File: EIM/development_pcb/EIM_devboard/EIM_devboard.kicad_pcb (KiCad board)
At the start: 2 copper layers, 100 x 100 mm, 114 parts, among them IC1 TPL7407LADR, IC2 MC33660BEFR2, J1 MX34028NF2, J2 Relays, J3 FTDI, J4 DB9_Male, J5 CAN, Q1 2N7000, Q10 2N7000, Q2 2N7000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

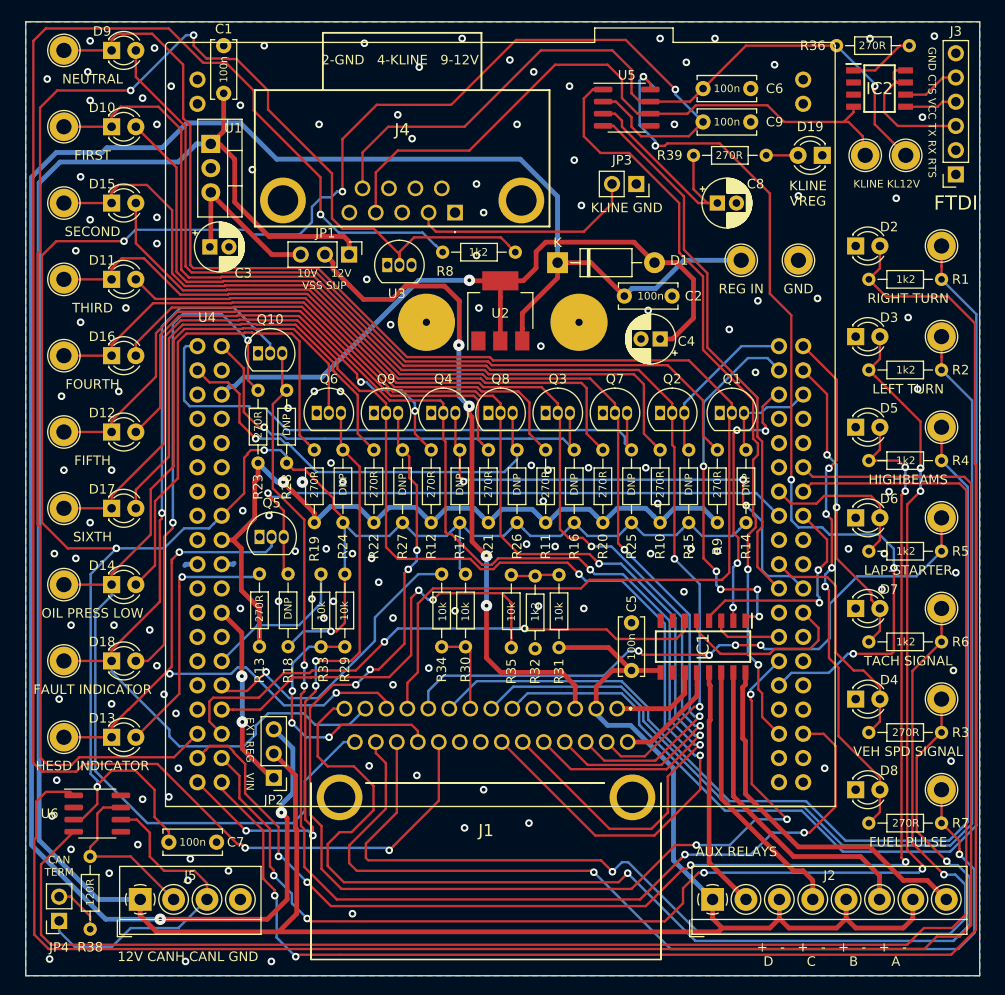
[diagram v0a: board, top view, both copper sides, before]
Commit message: Ordered version of EIM dev board
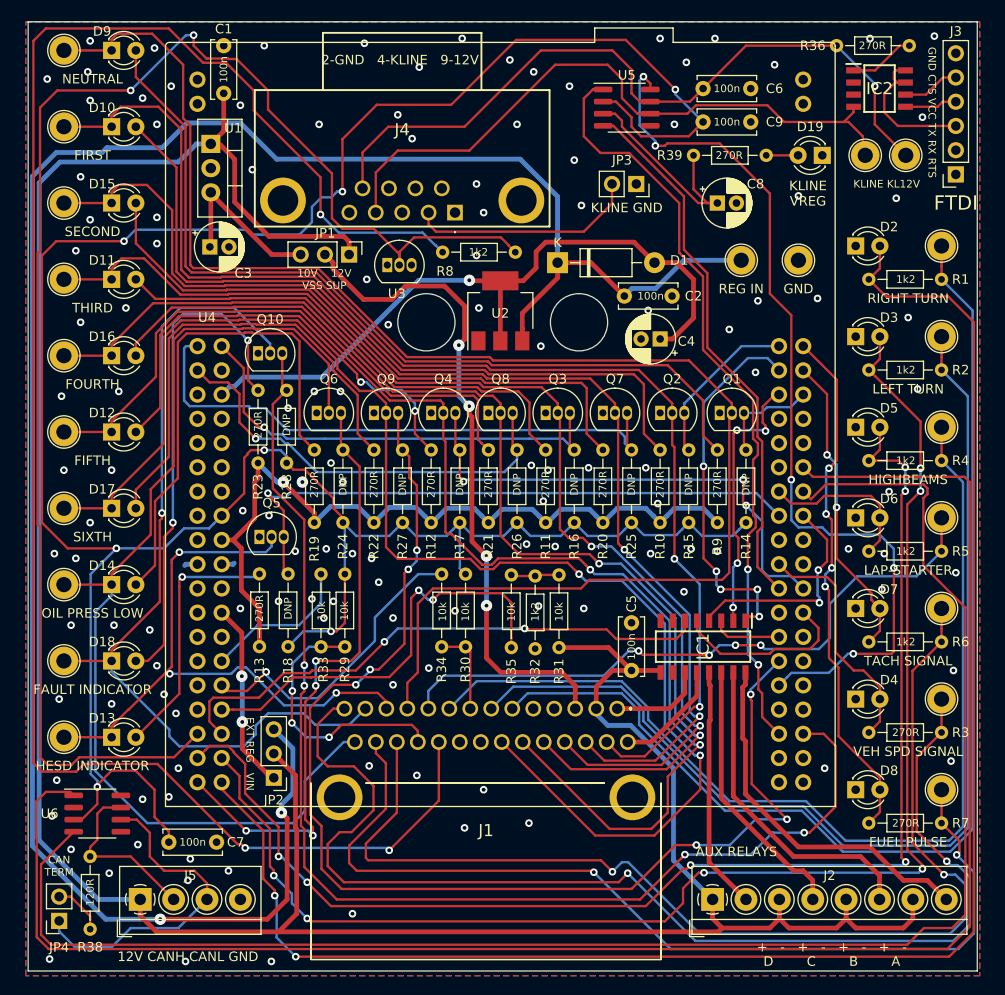
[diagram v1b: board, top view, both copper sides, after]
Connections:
- net /~MCP2021_FLT renamed /~{MCP2021_FLT}
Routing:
- net /~{MCP2021_FLT}: track 97.6 -> 95.5 mm
- net /CAN_RX: track 173.1 -> 171.7 mm
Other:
- board size 100 x 100 mm -> 99.5 x 99.5 mm
- net class Default removed
- net class RELAY removed
